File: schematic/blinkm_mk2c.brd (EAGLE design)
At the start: 15.2 x 23.4 mm, 16 parts, among them CN1 1X4SMT, U1 ATTINY44QFN

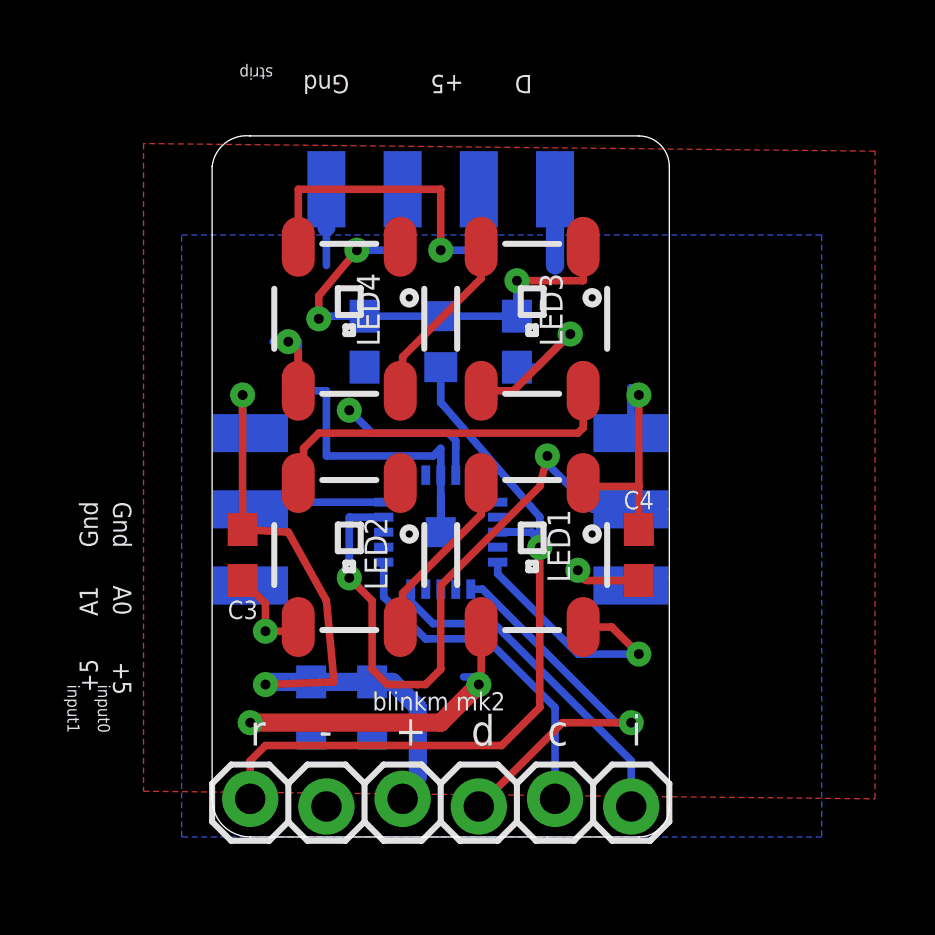
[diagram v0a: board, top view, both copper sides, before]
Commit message: updated blinkm_mk2c board layout, fully routed
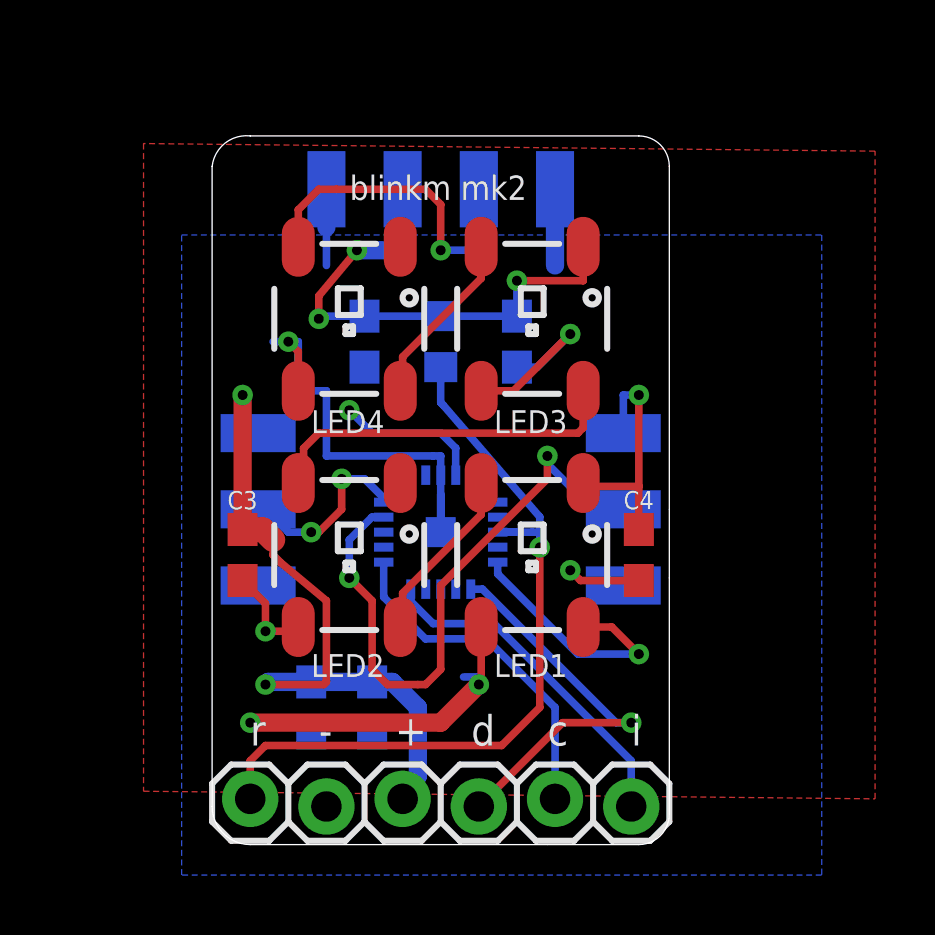
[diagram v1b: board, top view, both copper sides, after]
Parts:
- moved JP1 0.25 mm to (13.7, 10.9)
- moved JP2 0.25 mm to (1.52, 10.9)
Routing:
- net A0: track 4.54 -> 6.24 mm, vias 0 -> 2
- net DO: track 12.0 -> 11.3 mm
- net A1: track 21.4 -> 20.8 mm
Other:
- board size 15.2 x 23.4 mm -> 15.2 x 23.6 mm
- board text added: "DO"
- board text removed: "D"

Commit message: sync
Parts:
- added TP1, TP2: TEST-POINT3, SparkFun-Passives:PAD.03X.03
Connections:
- net DI: now also TP1.P$1
- net GND: now also TP2.P$1
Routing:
- net N$2: track 12.1 -> 10.8 mm
- net GND: track 44.1 -> 43.0 mm
- net RESET: track 26.3 -> 25.5 mm
- net +5V: track 55.0 -> 54.4 mm
- net DI: track 8.43 -> 8.97 mm
